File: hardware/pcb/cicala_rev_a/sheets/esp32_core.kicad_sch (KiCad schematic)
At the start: 28 parts, among them J4 TC2030 recovery pads, SW1 CATEGORY KSC321GLFS, SW2 NEXT KSC321GLFS, U1 ESP32-S3-WROOM-1-N16 / WROOM-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

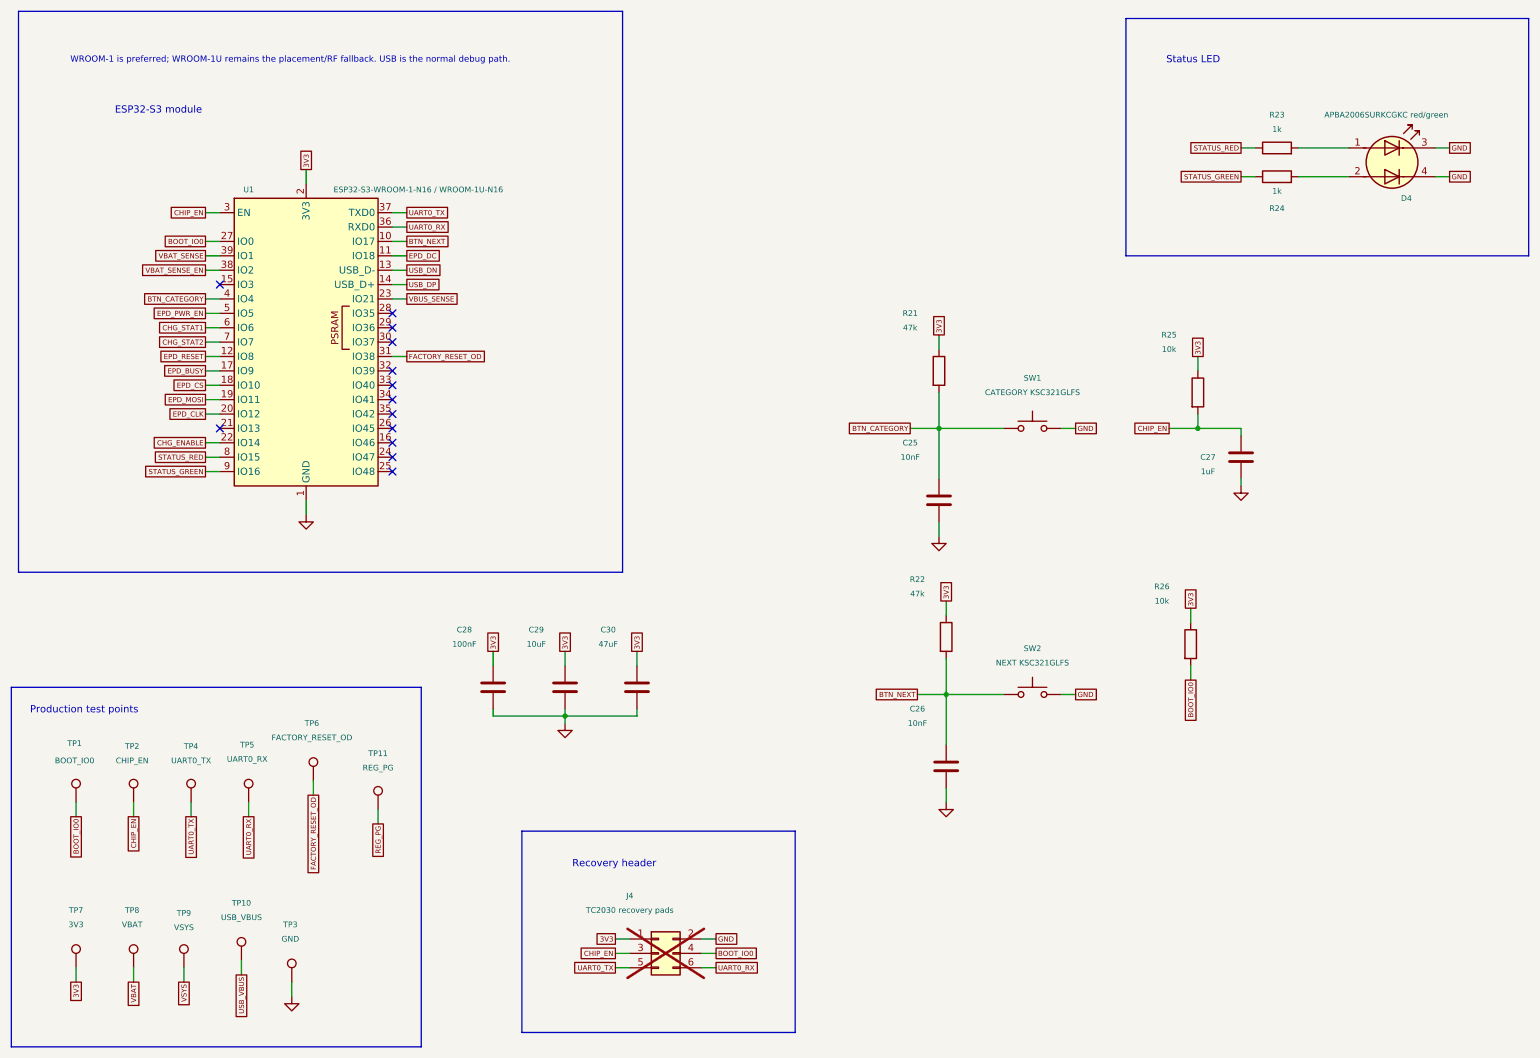
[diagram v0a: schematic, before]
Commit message: fix(hw): split the shorted USB pair and PREVGL pump node
Sheet re-layout that also separates two nets that were tied together.

J1 CC2, D+ and D- shared one net with both USBLC6 line pins; D+ and D-
are now their own nets. D1 had both pins on EPD_PREVGL, shorting it out
of the charge pump; its cathode is now the pump node with C16.

Three net labels were lost in the move and are now auto-named:
BATT_NTC, BTN_CATEGORY and BTN_NEXT. pin_contract.csv and BOM.md still
name them, so they need restoring.

Co-Authored-By: Claude Opus 5 (1M context) <noreply@anthropic.com>
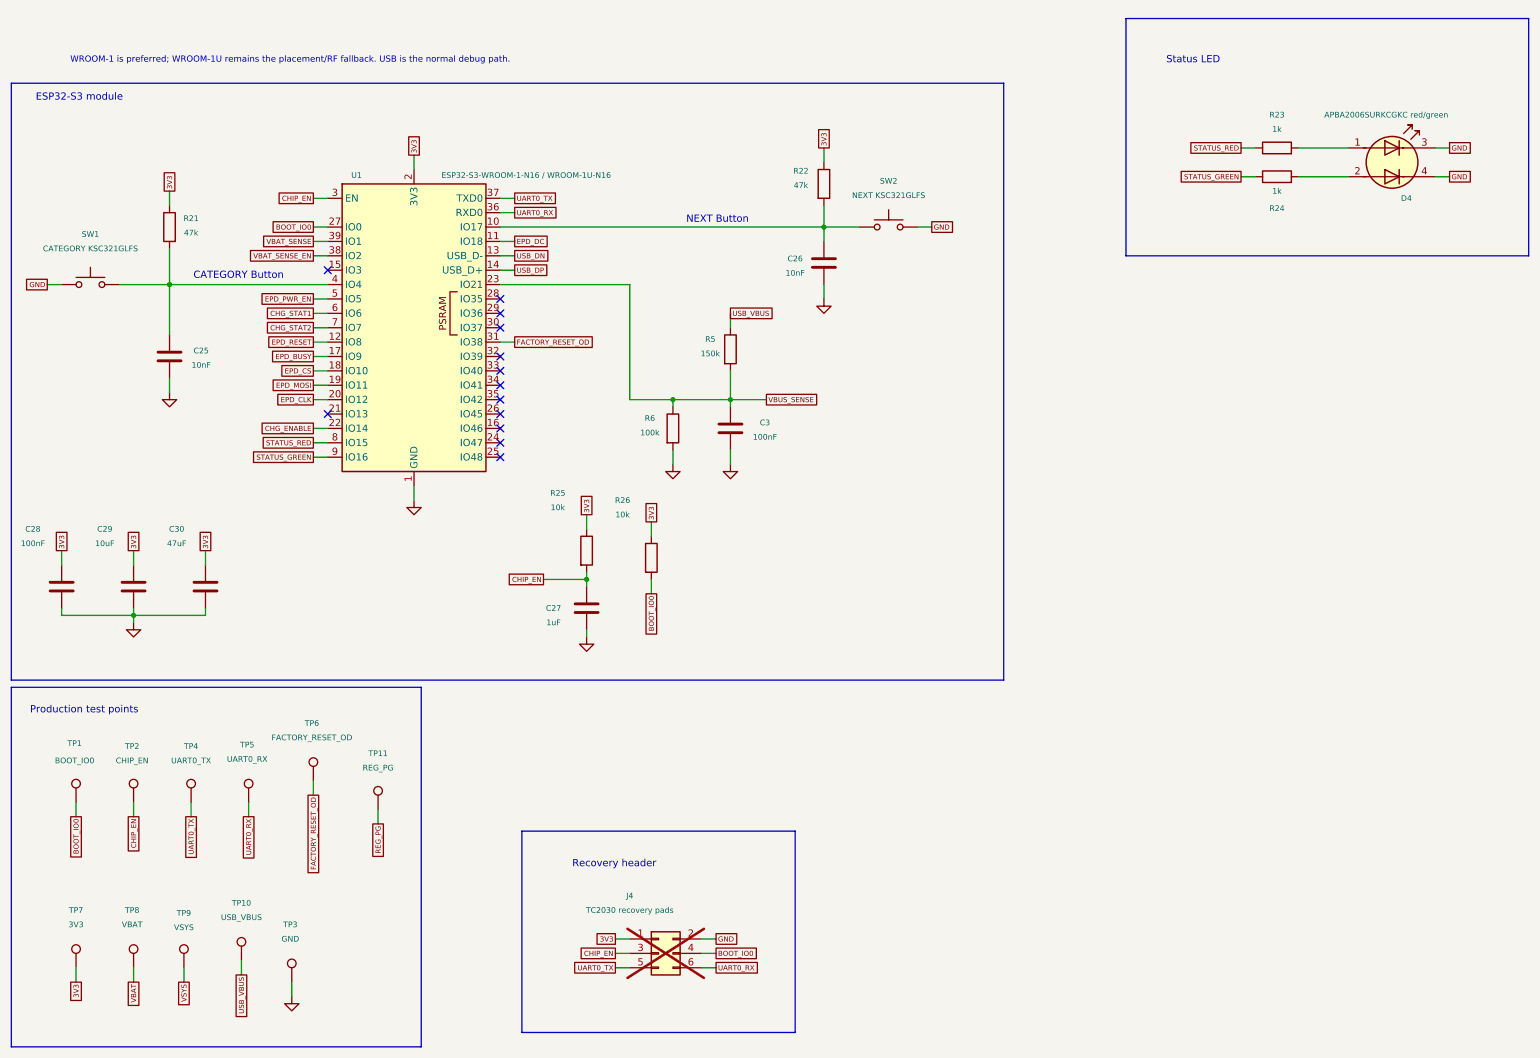
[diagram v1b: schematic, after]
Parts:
- added C3: 100nF, Capacitor_SMD:C_0603_1608Metric, symbol Device:C
- added R5: 150k, Resistor_SMD:R_0603_1608Metric, symbol Device:R
- added R6: 100k, Resistor_SMD:R_0603_1608Metric, symbol Device:R
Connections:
- net GND: now also C3.2, R6.2
- net USB_VBUS: now also R5.1
- net VBUS_SENSE: now also C3.1, R5.2, R6.1
- net BTN_CATEGORY: no longer names the net of C25.1, R21.2, SW1.1, U1.4 (IO4)
- net BTN_NEXT: no longer names the net of C26.1, R22.2, SW2.1, U1.10 (IO17)
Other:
- note added: "CATEGORY Button"
- note added: "NEXT Button"
- moved on the sheet: C25, C26, C27, C28, C29, C30, R21, R22, R25, R26, SW1, SW2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

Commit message: fix(hw): correct four ERC-invisible rev A wiring errors
All four are electrically valid connections that are simply wrong, which
is why ERC accepted them. Verified against the part datasheets and the
GDEY0213B74 reference circuit, and checked by re-exporting the netlist.

USB D+/D- were crossed between the receptacle and the MCU: J1 D- reached
GPIO20 (USB_D+) through U4 I/O1 and R3. Swapping the USB_DP and USB_DN
labels puts each line on its own pin without crossing wires. R3 now
carries D-, R4 carries D+.

Q1 used Q_NMOS_SGD, but the Si1308EDL in SOT-323 is pin 1 = G, 2 = S,
3 = D, so the gate driver landed on the sense node. The symbol is now
Q_NMOS_GSD; the drawing is unchanged because both symbols share the same
pin geometry.

D2's anode sat on EPD_PREVGL rather than on the pump node, leaving C16
with no charging path, so the negative rail could never develop. D1's
cathode, D2's anode and C16 now meet on EPD_PUMP, with D1 branching off
to EPD_PREVGL, as in the panel reference circuit.

C21 was 1 nF on VSH1, a driving rail the reference gives 1 uF/25 V.

Also restores three net names lost in the sheet re-layout: BATT_NTC,
BTN_CATEGORY and BTN_NEXT.

Co-Authored-By: Claude Opus 5 (1M context) <noreply@anthropic.com>
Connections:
- net BTN_NEXT: now reaches C26.1, R22.2, SW2.1, U1.10 (IO17)
- net BTN_CATEGORY: now reaches C25.1, R21.2, SW1.1, U1.4 (IO4)
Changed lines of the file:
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@@
+		)
+	)
+	(global_label "BTN_NEXT"
+		(shape passive)
+		(at 110.49 52.07 0)
+		(fields_autoplaced yes)
+		(effects
+			(font
+				(size 0.9 0.9)
+			)
+			(justify left)
+		)
+		(property "Intersheetrefs" "${INTERSHEET_REFS}"
+			(at 110.49 52.07 0)
+			(hide yes)
+			(show_name no)
+			(do_not_autoplace no)
+			(effects
+				(font
+					(size 0.8 0.8)
+				)
+			)
+		)
+	)
+	(global_label "BTN_CATEGORY"
+		(shape passive)
+		(at 45.72 62.23 0)
+		(fields_autoplaced yes)
+		(effects
+			(font
+				(size 0.9 0.9)
+			)
+			(justify left)
+		)
+		(property "Intersheetrefs" "${INTERSHEET_REFS}"
+			(at 45.72 62.23 0)
+			(hide yes)
+			(show_name no)
+			(do_not_autoplace no)
+			(effects
+				(font
+					(size 0.8 0.8)
+				)
+			)
 		)
 	)

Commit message: style(hw): tidy the rev A sheet layout
Component and label placement only. The exported netlist and BOM are
identical to the previous commit, and ERC, DRC and STEP export pass.

Co-Authored-By: Claude Opus 5 (1M context) <noreply@anthropic.com>
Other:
- note removed: "CATEGORY Button"
- note removed: "NEXT Button"

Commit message: fix(hw): correct the VBUS divider and the TPS22917 slew capacitor
R5 and R6 were the wrong way round: 150 k from VBUS to the sense node over
100 k to ground gives 2.0 V from a 5 V bus, below the ESP32-S3 guaranteed
high-input threshold at 3.3 V. Swapping them gives 3.0 V, which is what the
DevKitC overlay already assumes.

C14 returned to GND. The TPS22917 slew capacitor is referenced to VIN, not
GND (SLVSDW8B section 9.3.2, "A capacitor to VIN on the CT pin sets the slew
rate of VOUT"), so its far side moves to the U6 3V3 input rail.

Neither error was visible to ERC; both are electrically valid connections
that compute the wrong answer.

Co-Authored-By: Claude Opus 5 <noreply@anthropic.com>
Claude-Session: https://claude.ai/code/session_01E5vy1HJsPztSk9nFw6j5Ko
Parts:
- R5: value 150k -> 100k
- R6: value 100k -> 150k
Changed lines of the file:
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@@
 			)
 		)
-		(property "Value" "100k"
+		(property "Value" "150k"
 			(at 126.746 88.392 0)
 			(show_name no)
@@
 			)
 		)
-		(property "Value" "150k"
+		(property "Value" "100k"
 			(at 137.414 74.422 0)
 			(show_name no)

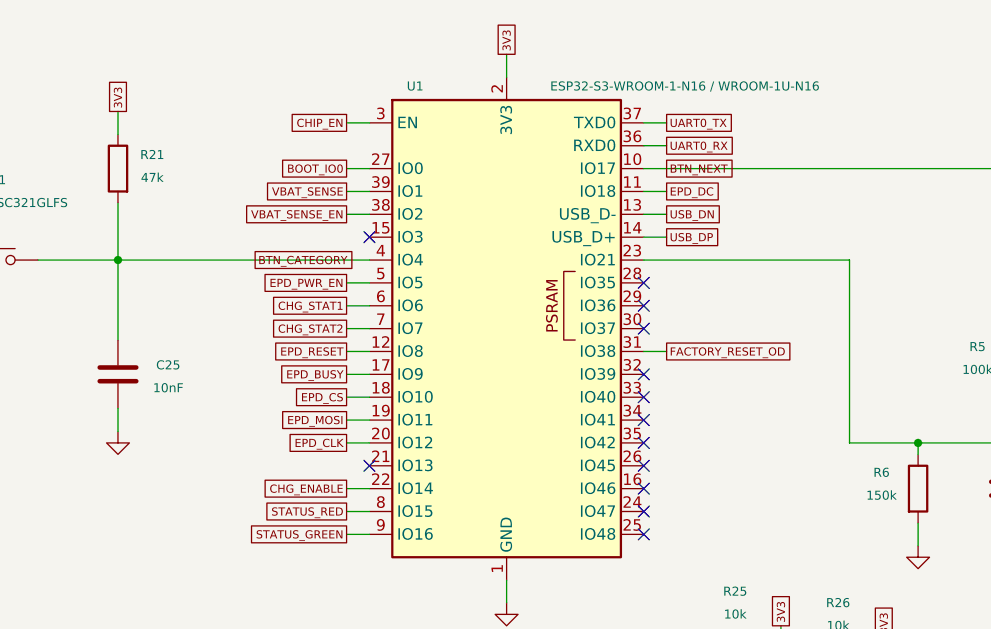
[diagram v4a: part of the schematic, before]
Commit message: feat(hw): isolate the panel bus and ground the USB-C shell
The panel's logic pins could back-power an unpowered panel through its own
ESD diodes whenever firmware deasserted EPD_PWR_EN with an output still
driven. R27-R31 put 470 ohm in series with every MCU-driven panel line, which
caps the injected current at about 5.7 mA per pin against a 3.3 V output and
a diode drop. At 4 MHz into roughly 20 pF of connector and trace the added
rise time is about 21 ns, so the same parts double as the series-tuning
positions the review asked for; fit 0 ohm to remove them during bring-up.

R32 holds the panel in reset while EPD_3V3 is off and while the MCU pin is
high-impedance. 1 M draws 3.3 uA, and only when RESET is high, which happens
only with the panel already powered.

The nets either side of the resistors are named apart: EPD_* stays the GPIO
net that pin_contract.csv and the firmware refer to, PNL_* is the panel side.

The USB-C shell had a no-connect flag and no recorded rationale. The
enclosure is plastic and carries no chassis ground, so the shell's only
discharge path is to the board. R33 (0 ohm, fitted) makes that path direct;
C31 is the alternative for a DC-isolated shell.

Co-Authored-By: Claude Opus 5 <noreply@anthropic.com>
Claude-Session: https://claude.ai/code/session_01E5vy1HJsPztSk9nFw6j5Ko
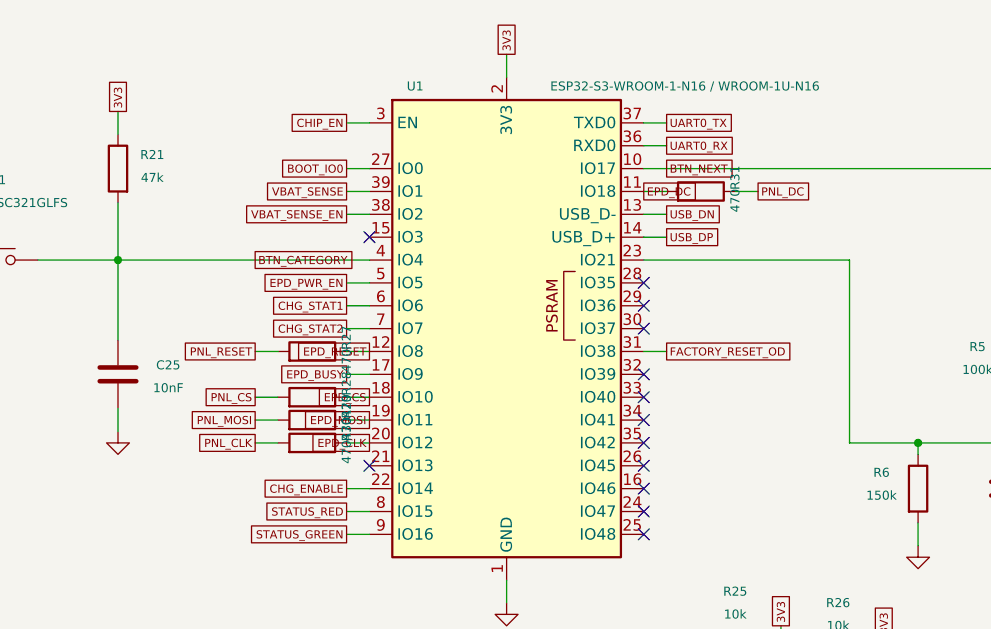
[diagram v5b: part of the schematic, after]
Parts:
- added R27, R28, R29, R30, R31: 470, Resistor_SMD:R_0603_1608Metric, symbol Device:R
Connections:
- net EPD_CLK: now also R30.1
- net EPD_CS: now also R28.1
- net EPD_DC: now also R31.2
- net EPD_MOSI: now also R29.1
- net EPD_RESET: now also R27.1
- new net PNL_CLK: R30.2
- new net PNL_CS: R28.2
- new net PNL_DC: R31.1
- new net PNL_MOSI: R29.2
- new net PNL_RESET: R27.2

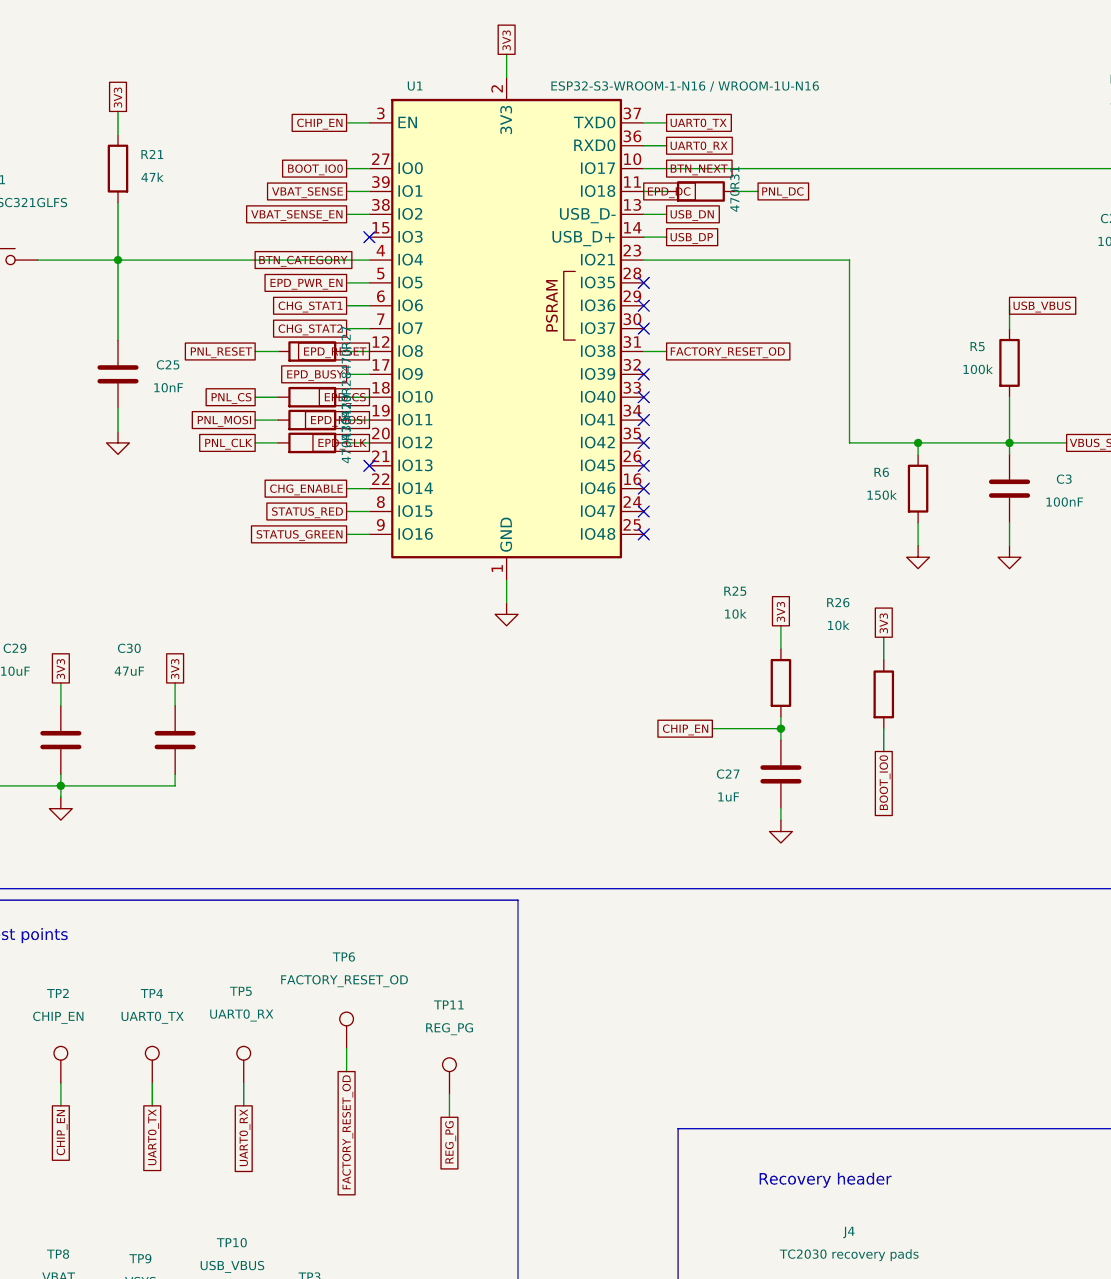
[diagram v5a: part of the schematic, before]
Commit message: feat(hw): add the production test contract and a cell-current link
TP12-TP15 expose the USB pair and both charger status lines. TP16-TP21 expose
the panel side of the display bus, next to the isolation resistors that now
live on the panel sheet where the interface they protect is drawn.

R34 is a removable 0 ohm link in the cell lead, with TP22 on the pack side.
Lifting it puts a meter between the pack and everything else, which is the
only way to measure whole-device sleep current against the 30 uA target
without cutting a trace. No link is placed in a switching loop: VSYS and 3V3
stay unbroken and are probed at TP7 and TP9.

Co-Authored-By: Claude Opus 5 <noreply@anthropic.com>
Claude-Session: https://claude.ai/code/session_01E5vy1HJsPztSk9nFw6j5Ko
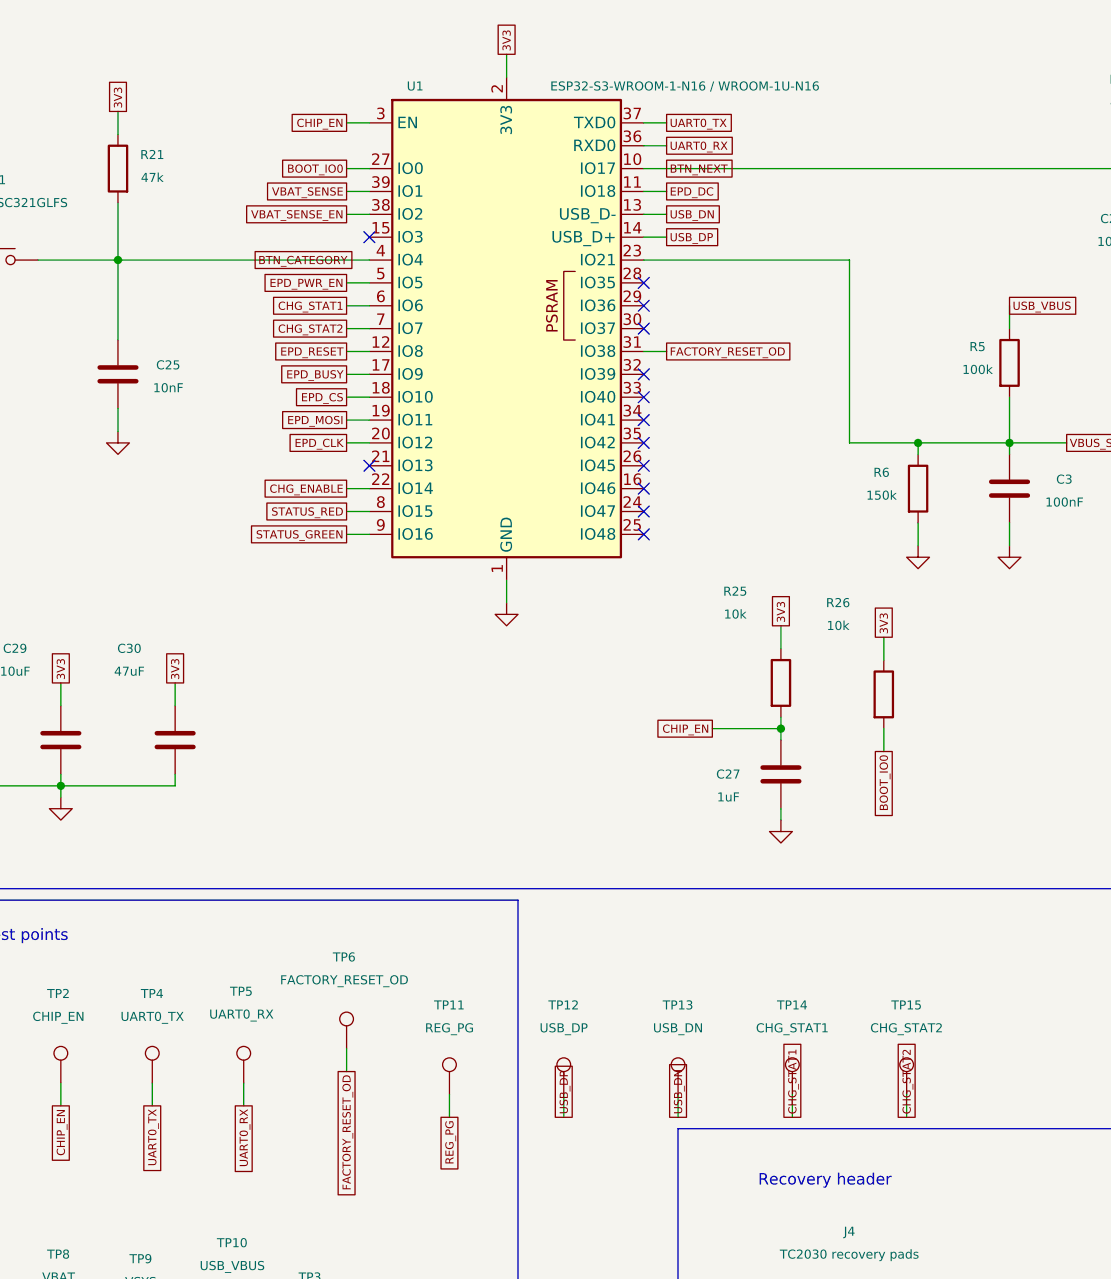
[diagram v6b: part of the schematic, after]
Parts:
- removed R27, R28, R29, R30, R31: 470, Resistor_SMD:R_0603_1608Metric, symbol Device:R
- added TP12: USB_DP, TestPoint:TestPoint_Pad_D1.0mm, symbol Connector:TestPoint
- added TP13: USB_DN, TestPoint:TestPoint_Pad_D1.0mm, symbol Connector:TestPoint
- added TP14: CHG_STAT1, TestPoint:TestPoint_Pad_D1.0mm, symbol Connector:TestPoint
- added TP15: CHG_STAT2, TestPoint:TestPoint_Pad_D1.0mm, symbol Connector:TestPoint
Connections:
- net CHG_STAT1: now also TP14.1
- net CHG_STAT2: now also TP15.1
- net USB_DN: now also TP13.1
- net USB_DP: now also TP12.1
